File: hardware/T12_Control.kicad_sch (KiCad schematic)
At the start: 34 parts, among them J1 Screw_Terminal_01x02, J2 GX12-5M, J3 Conn_01x07_Female, J4 Conn_01x04_Female, J5 Conn_01x06_Male, J6 Conn_01x04_Male, Q1 TPC8107, Q2 SI2308A, U1 LF15_TO252, U2 24LC32, U3 SGM8551XN, U4 STM32F103CBTx

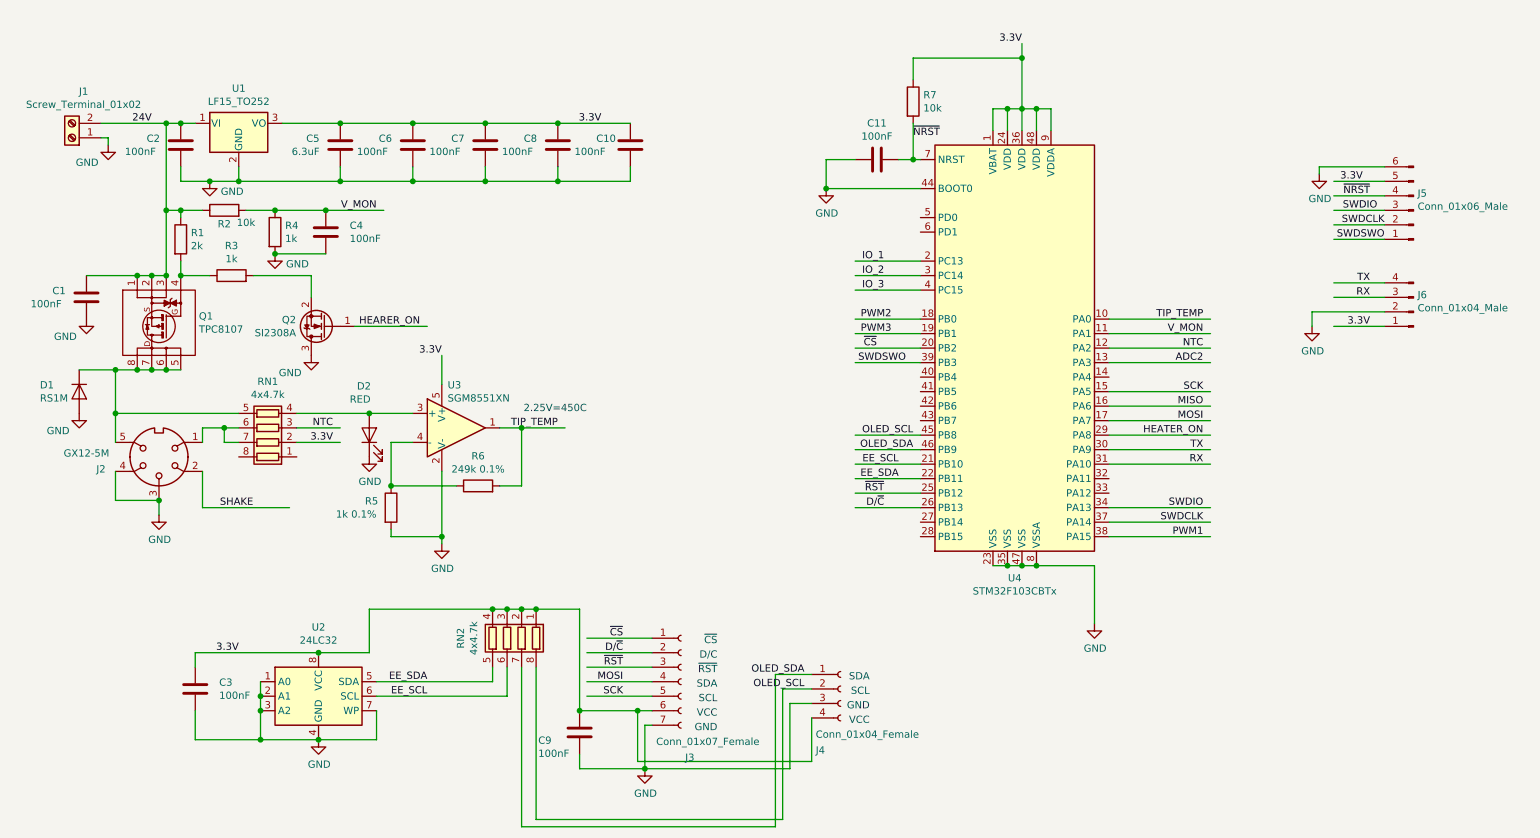
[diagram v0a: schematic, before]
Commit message: Routhe the T12 Iron controller.
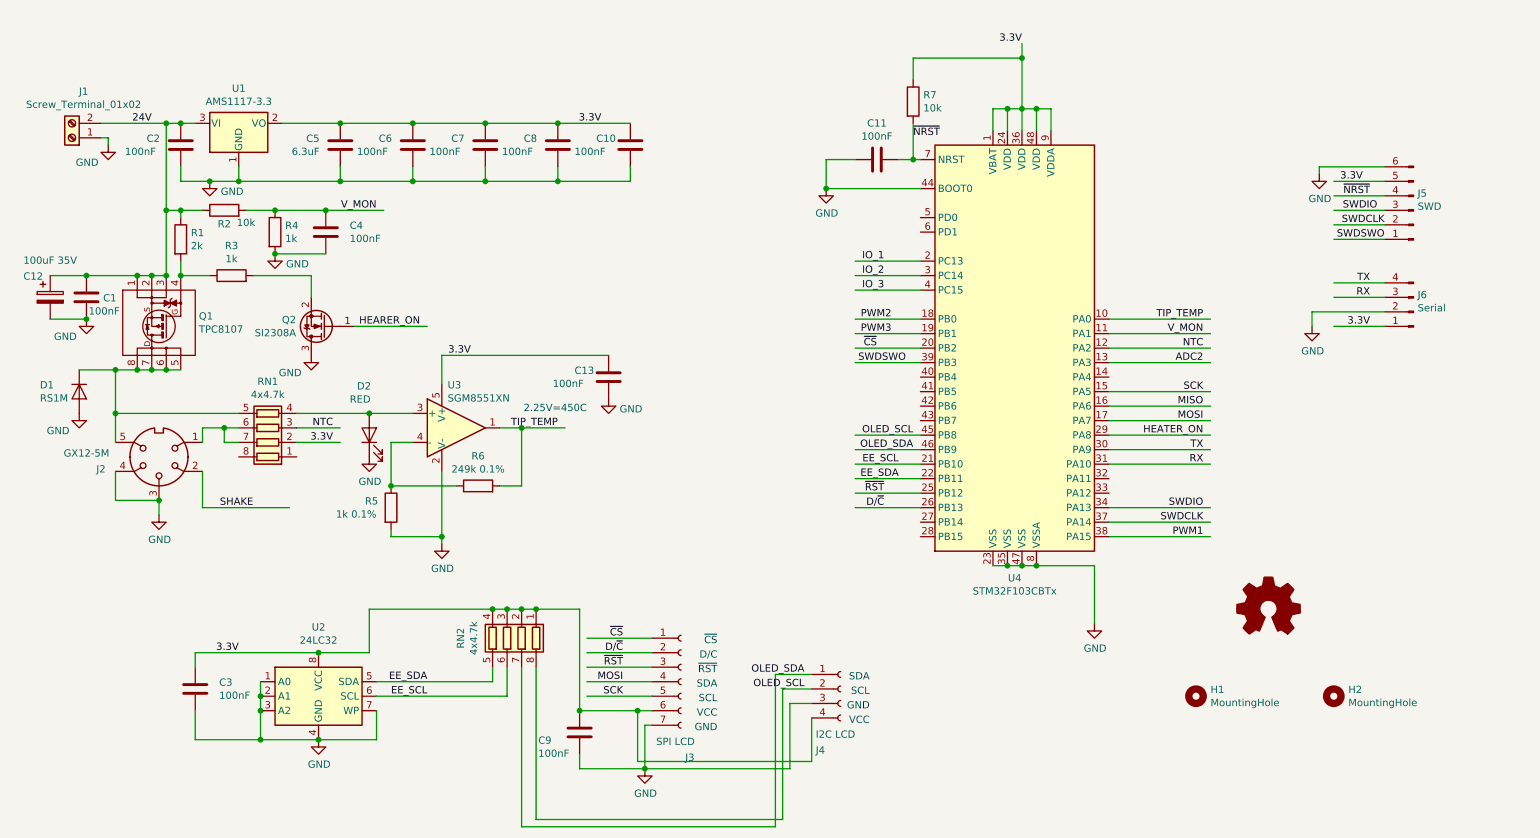
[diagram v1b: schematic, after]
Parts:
- removed U1: LF15_TO252, Package_TO_SOT_SMD:TO-252-2, symbol Regulator_Linear:LF15_TO252
- added C12: 100uF 35V, Capacitor_SMD:CP_Elec_6.3x7.7, symbol Device:CP
- added C13: 100nF, Capacitor_SMD:C_0603_1608Metric, symbol Device:C
- added H1, H2: MountingHole, MountingHole:MountingHole_3.2mm_M3_DIN965, symbol Mechanical:MountingHole
- added U1: AMS1117-3.3, Package_TO_SOT_SMD:SOT-223-3_TabPin2, symbol Regulator_Linear:AMS1117-3.3
- J2: footprint (none) -> Connector_Wago:Wago_734-135_1x05_P3.50mm_Vertical
- J3: value Conn_01x07_Female -> SPI LCD
- J4: value Conn_01x04_Female -> I2C LCD
- J5: value Conn_01x06_Male -> SWD
- J6: value Conn_01x04_Male -> Serial
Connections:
- net 24V: now also C12.1, U1.3 (VI)
- net 3.3V: now also C13.1, U1.2 (VO)
- net GND: now also C12.2, C13.2, U1.1 (GND)

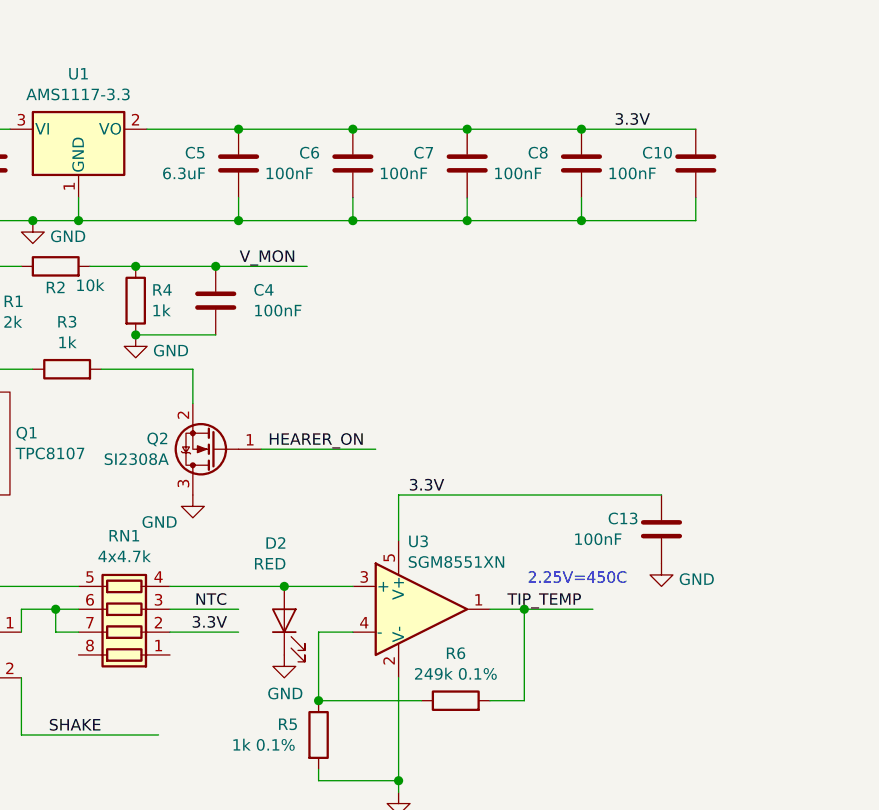
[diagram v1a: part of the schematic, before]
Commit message: Added LCSC Part #s Generated fab files.
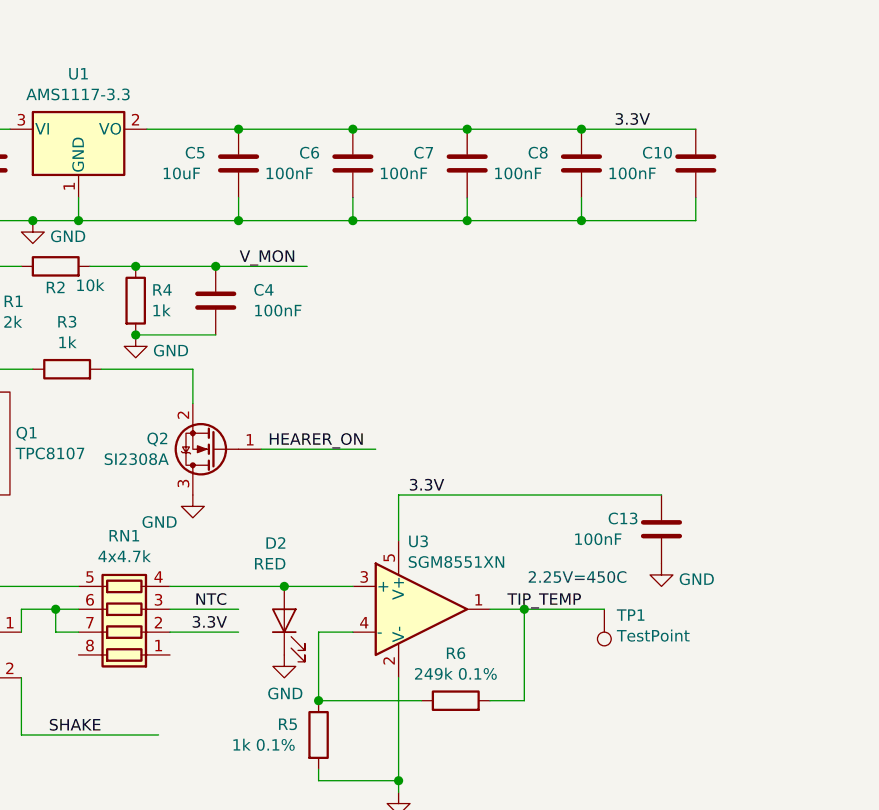
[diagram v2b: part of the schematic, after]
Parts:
- added TP1: TestPoint, TestPoint:TestPoint_Pad_D1.0mm, symbol Connector:TestPoint
- C1, C10, C11, C13, C2, C3, C4, C6, C7, C8, C9: LCSC Part# (none) -> C14663
- C12: LCSC Part# (none) -> C134792
- C5: value 6.3uF -> 10uF; LCSC Part# (none) -> C96446
- D1: LCSC Part# (none) -> C181126
- D2: LCSC Part# (none) -> C2286
- J1, J2, J3, J4, J5, J6: now left out of the parts list
- Q1: LCSC Part# (none) -> C710107
- Q2: LCSC Part# (none) -> C12298
- R1, R3, R4, R5: LCSC Part# (none) -> C22975
- R2, R7: LCSC Part# (none) -> C25804
- R6: LCSC Part# (none) -> C22918
- RN1, RN2: footprint Resistor_SMD:R_Array_Concave_4x0402 -> Resistor_SMD:R_Array_Concave_4x0603; LCSC Part# (none) -> C181126
- U1: LCSC Part# (none) -> C6186
- U2: LCSC Part# (none) -> C511262
- U3: LCSC Part# (none) -> C83748
- U4: LCSC Part# (none) -> C8304
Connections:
- net TIP_TEMP: now also TP1.1

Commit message: Revert the resistor networks back to 4x0402 footprint, not using JLC assembly svc for now.
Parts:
- RN1, RN2: footprint Resistor_SMD:R_Array_Concave_4x0603 -> Resistor_SMD:R_Array_Concave_4x0402
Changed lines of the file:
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@@
     (property "Reference" "RN1" (id 0) (at 55.88 90.9382 90))
     (property "Value" "4x4.7k" (id 1) (at 55.88 93.237 90))
-    (property "Footprint" "Resistor_SMD:R_Array_Concave_4x0603" (id 2) (at 55.88 92.075 90)
+    (property "Footprint" "Resistor_SMD:R_Array_Concave_4x0402" (id 2) (at 55.88 92.075 90)
       (effects (font (size 1.27 1.27)) hide)
     )
@@
     (property "Reference" "RN2" (id 0) (at 89.6682 135.89 90))
     (property "Value" "4x4.7k" (id 1) (at 91.967 135.89 90))
-    (property "Footprint" "Resistor_SMD:R_Array_Concave_4x0603" (id 2) (at 90.805 135.89 90)
+    (property "Footprint" "Resistor_SMD:R_Array_Concave_4x0402" (id 2) (at 90.805 135.89 90)
       (effects (font (size 1.27 1.27)) hide)
     )
@@
     )
     (path "/690fbdb1-74ee-40cb-b615-e8cc50944501"
-      (reference "RN1") (unit 1) (value "4x4.7k") (footprint "Resistor_SMD:R_Array_Concave_4x0603")
+      (reference "RN1") (unit 1) (value "4x4.7k") (footprint "Resistor_SMD:R_Array_Concave_4x0402")
     )
     (path "/c3ab5ec6-bd2f-4109-bfdd-092055883123"
-      (reference "RN2") (unit 1) (value "4x4.7k") (footprint "Resistor_SMD:R_Array_Concave_4x0603")
+      (reference "RN2") (unit 1) (value "4x4.7k") (footprint "Resistor_SMD:R_Array_Concave_4x0402")
     )
     (path "/a0744780-e430-46ed-8424-2fd4bcfa4fc4"

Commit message: Update the 1N4148 diodes to B5819W. The 1N was too puny to serve as protection.
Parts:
- Q1: footprint Package_SO:SO-8_5.3x6.2mm_P1.27mm -> Package_SO:SO-8_3.9x4.9mm_P1.27mm
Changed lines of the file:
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@@
       (effects (font (size 1.27 1.27)) (justify left))
     )
-    (property "Footprint" "Package_SO:SO-8_5.3x6.2mm_P1.27mm" (id 2) (at 36.5252 90.8304 0)
+    (property "Footprint" "Package_SO:SO-8_3.9x4.9mm_P1.27mm" (id 2) (at 36.5252 90.8304 0)
       (effects (font (size 1.27 1.27)) hide)
     )
@@
     )
     (path "/0d2a404f-024a-4ffe-b0c5-80a1d2737d76"
-      (reference "Q1") (unit 1) (value "TPC8107") (footprint "Package_SO:SO-8_5.3x6.2mm_P1.27mm")
+      (reference "Q1") (unit 1) (value "TPC8107") (footprint "Package_SO:SO-8_3.9x4.9mm_P1.27mm")
     )
     (path "/f0e989e3-5869-42b0-8413-f4ce97a63781"

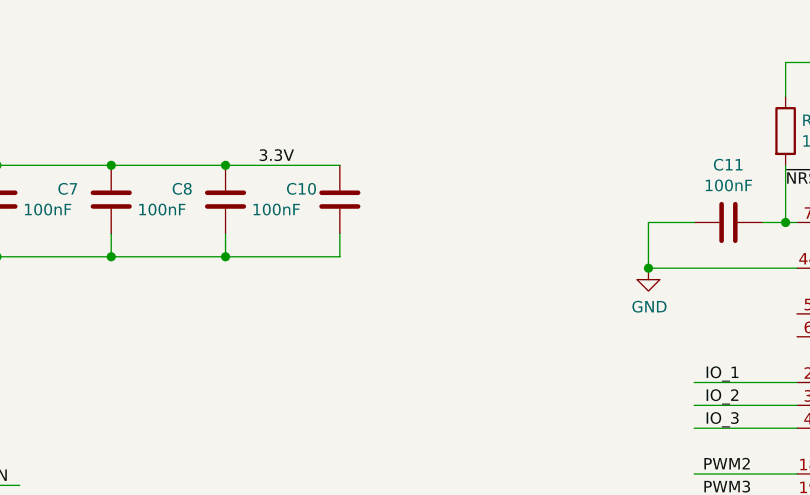
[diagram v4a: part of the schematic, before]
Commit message: Rotate the display connectors 180 degrees. Add extra filter cap on pin 1 (VBAT). Improve PCB layout.
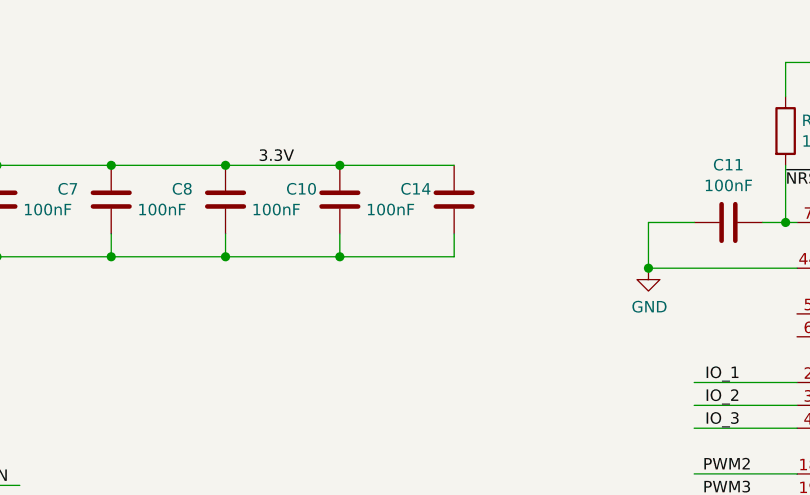
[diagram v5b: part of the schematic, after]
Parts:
- added C14: 100nF, Capacitor_SMD:C_0603_1608Metric, symbol Device:C
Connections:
- net 3.3V: now also C14.1
- net GND: now also C14.2
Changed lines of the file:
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@@
 (kicad_sch (version 20201015) (generator eeschema)
-  (page 1 1)
   (paper "A4")
   (junction (at 24.13 72.39) (diameter 1.016) (color 0 0 0 0))
@@
   (junction (at 106.68 55.88) (diameter 1.016) (color 0 0 0 0))
   (junction (at 110.49 148.59) (diameter 1.016) (color 0 0 0 0))
+  (junction (at 119.38 45.72) (diameter 1.016) (color 0 0 0 0))
+  (junction (at 119.38 55.88) (diameter 1.016) (color 0 0 0 0))
   (junction (at 120.65 148.59) (diameter 1.016) (color 0 0 0 0))
   (junction (at 121.92 158.75) (diameter 1.016) (color 0 0 0 0))
@@
     (stroke (width 0) (type solid) (color 0 0 0 0))
   )
+  (wire (pts (xy 119.38 45.72) (xy 132.08 45.72))
+    (stroke (width 0) (type solid) (color 0 0 0 0))
+  )
   (wire (pts (xy 119.38 53.34) (xy 119.38 55.88))
     (stroke (width 0) (type solid) (color 0 0 0 0))
@@
   )
   (wire (pts (xy 121.92 151.13) (xy 123.19 151.13))
+    (stroke (width 0) (type solid) (color 0 0 0 0))
+  )
+  (wire (pts (xy 132.08 53.34) (xy 132.08 55.88))
+    (stroke (width 0) (type solid) (color 0 0 0 0))
+  )
+  (wire (pts (xy 132.08 55.88) (xy 119.38 55.88))
     (stroke (width 0) (type solid) (color 0 0 0 0))
   )
@@
     )
   )
+  (symbol (lib_id "Device:C") (at 132.08 49.53 0) (unit 1)
+    (in_bom yes) (on_board yes)
+    (property "Reference" "C14" (id 0) (at 126.1111 48.3806 0)
+      (effects (font (size 1.27 1.27)) (justify left))
+    )
+    (property "Value" "100nF" (id 1) (at 122.301 50.679 0)
+      (effects (font (size 1.27 1.27)) (justify left))
+    )
+    (property "Footprint" "Capacitor_SMD:C_0603_1608Metric" (id 2) (at 133.0452 53.34 0)
+      (effects (font (size 1.27 1.27)) hide)
+    )
+    (property "Datasheet" "~" (id 3) (at 132.08 49.53 0)
+      (effects (font (size 1.27 1.27)) hide)
+    )
+    (property "LCSC Part#" "C14663" (id 4) (at 53.34 49.53 0)
+      (effects (font (size 1.27 1.27)) hide)
+    )
+  )
   (symbol (lib_id "Device:C") (at 162.56 52.07 90) (unit 1)
     (in_bom yes) (on_board yes)
@@
       (reference "C13") (unit 1) (value "100nF") (footprint "Capacitor_SMD:C_0603_1608Metric")
     )
+    (path "/a7792f94-cdd7-449a-9028-d240f726c413"
+      (reference "C14") (unit 1) (value "100nF") (footprint "Capacitor_SMD:C_0603_1608Metric")
+    )
     (path "/e69ef43c-7faf-4f6d-896b-445411405372"

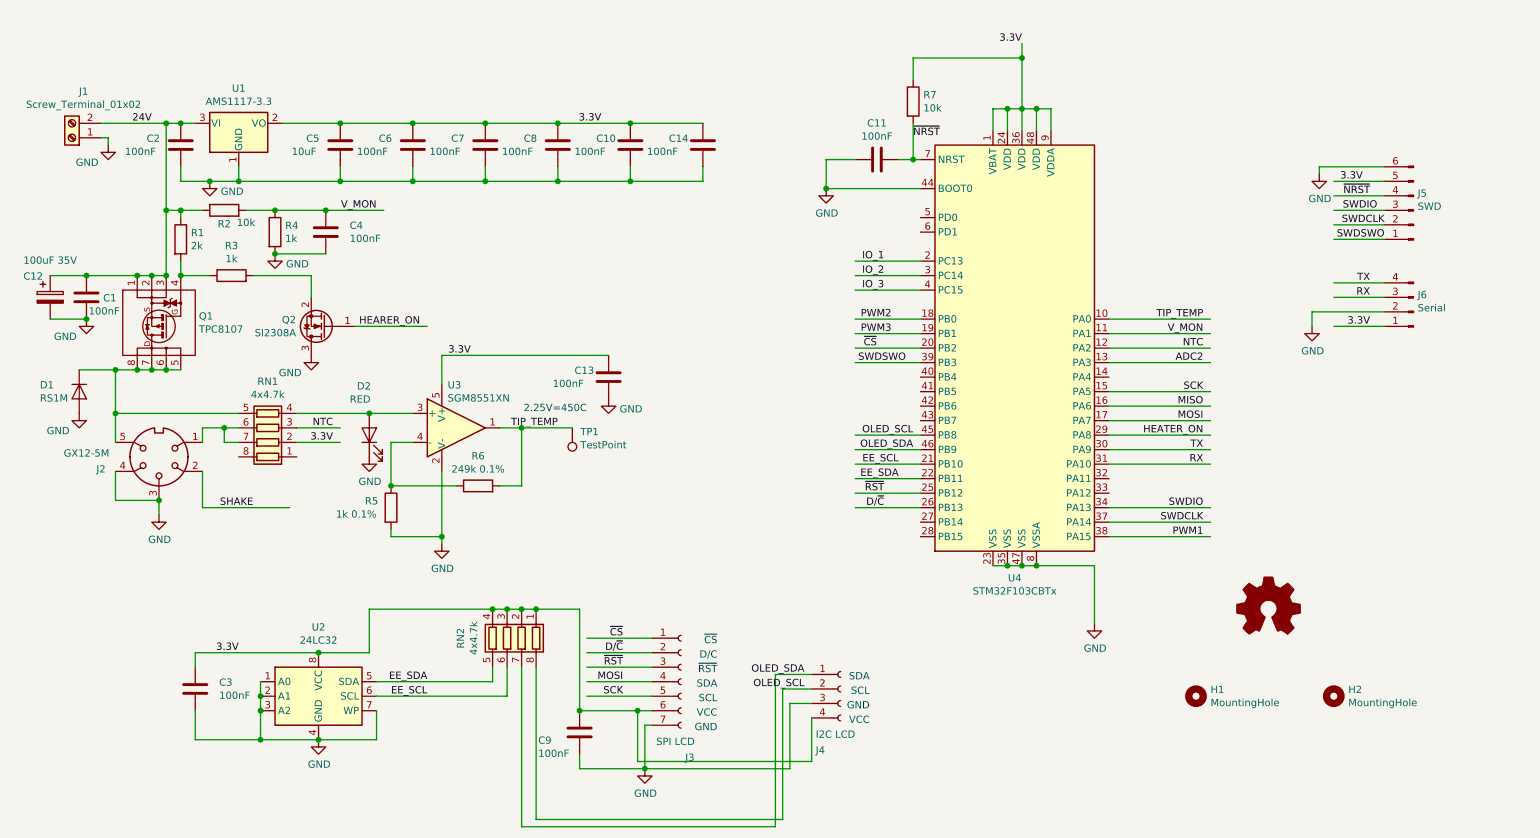
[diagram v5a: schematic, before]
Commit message: Updated soldering iron board.
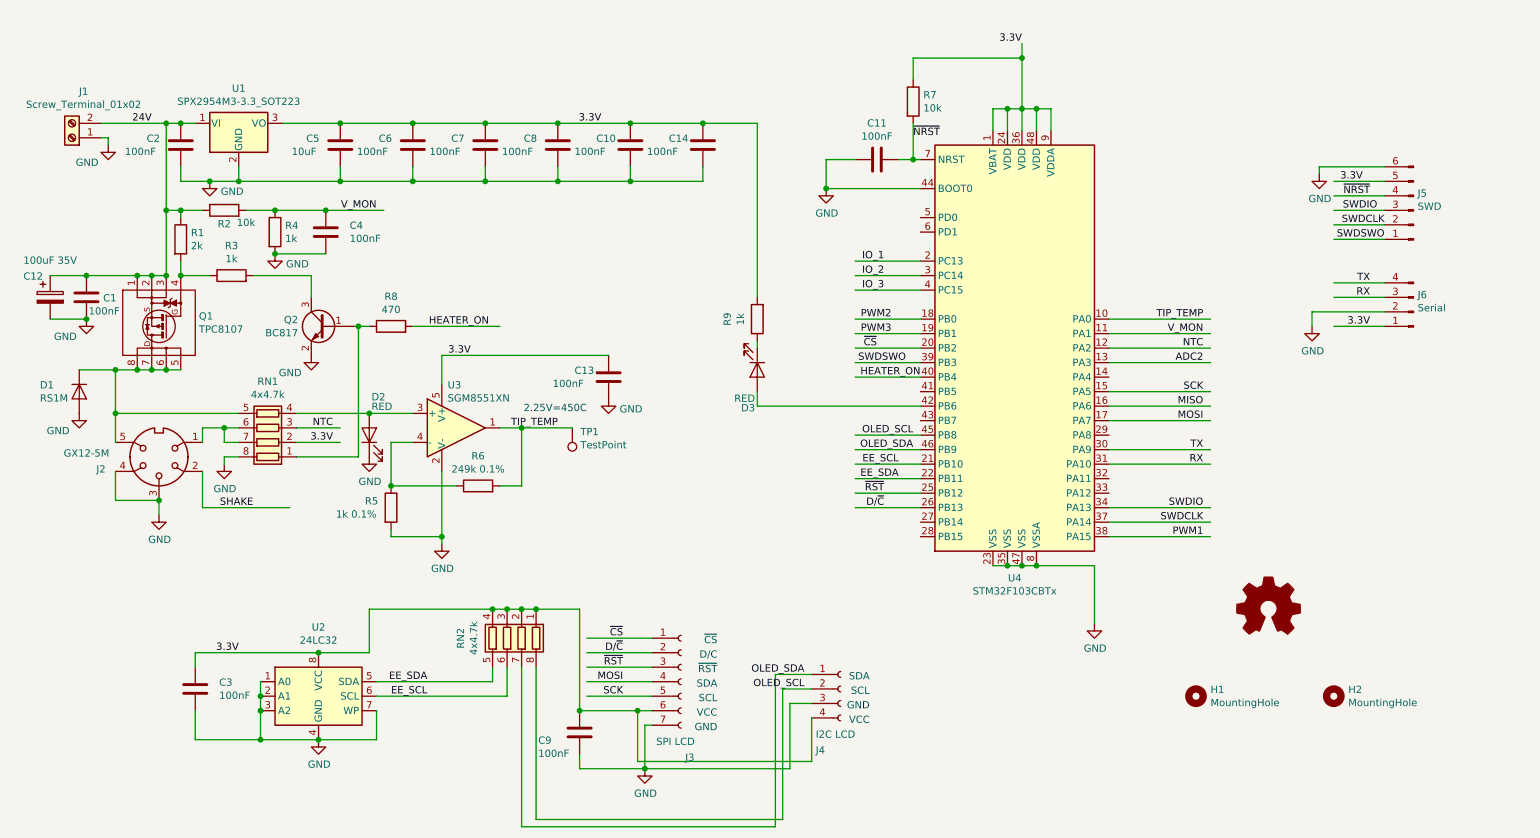
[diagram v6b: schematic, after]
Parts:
- removed Q2: SI2308A, Package_TO_SOT_SMD:SOT-23, symbol Device:Q_NMOS_GSD
- removed U1: AMS1117-3.3, Package_TO_SOT_SMD:SOT-223-3_TabPin2, symbol Regulator_Linear:AMS1117-3.3
- added D3: RED, LED_SMD:LED_0603_1608Metric, symbol Device:LED
- added Q2: BC817, Package_TO_SOT_SMD:SOT-23, symbol Transistor_BJT:BC817
- added R8: 470, Resistor_SMD:R_0603_1608Metric, symbol Device:R
- added R9: 1k, Resistor_SMD:R_0603_1608Metric, symbol Device:R
- added U1: SPX2954M3-3.3_SOT223, Package_TO_SOT_SMD:SOT-223-3_TabPin2, symbol Regulator_Linear:SPX2920M3-3.3_SOT223
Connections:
- net 24V: now also U1.1 (VI)
- net 3.3V: now also R9.2, U1.3 (VO)
- net GND: now also RN1.8 (R1.2), Q2.2 (E), U1.2 (GND)
- net HEATER_ON: now also U4.40 (PB4), R8.2; no longer U4.29 (PA8)
- net at R3.2: now also Q2.3 (C)
- net at RN1.1 (R1.1): now also Q2.1 (B), R8.1
- net at U4.42 (PB6): now also D3.2 (A)
- new net: D3.1 (K), R9.1
